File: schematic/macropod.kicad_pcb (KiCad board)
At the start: 2 copper layers, 97.5 x 113.5 mm, 52 parts, among them J1 USB_B_Micro, J2 Conn_ARM_JTAG_SWD_10, SW1 SW_MK, SW10 SW_MK, SW11 SW_MK, SW12 SW_MK, SW13 SW_MK, SW14 SW_MK, SW15 SW_MK, SW16 SW_MK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

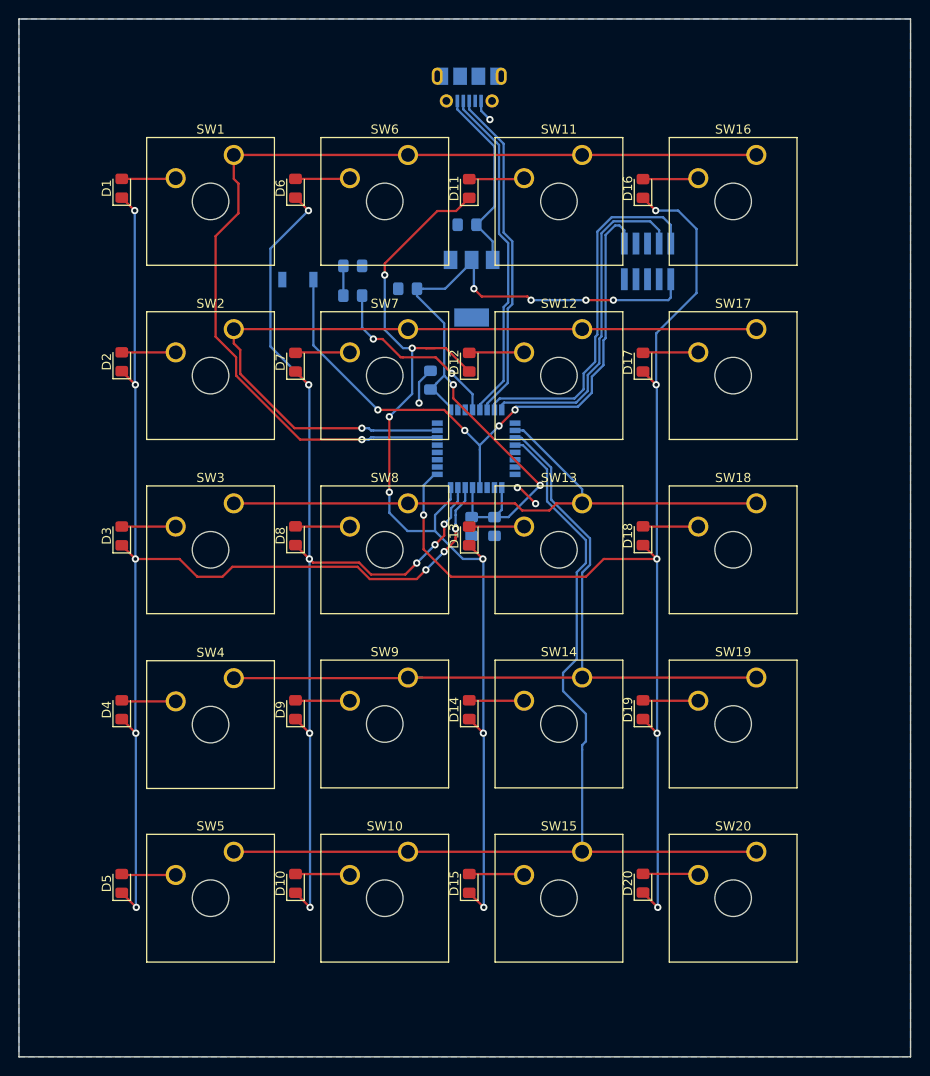
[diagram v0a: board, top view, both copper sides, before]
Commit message: Updated footprints to match BOM components. Applied DRC settings for fabrication
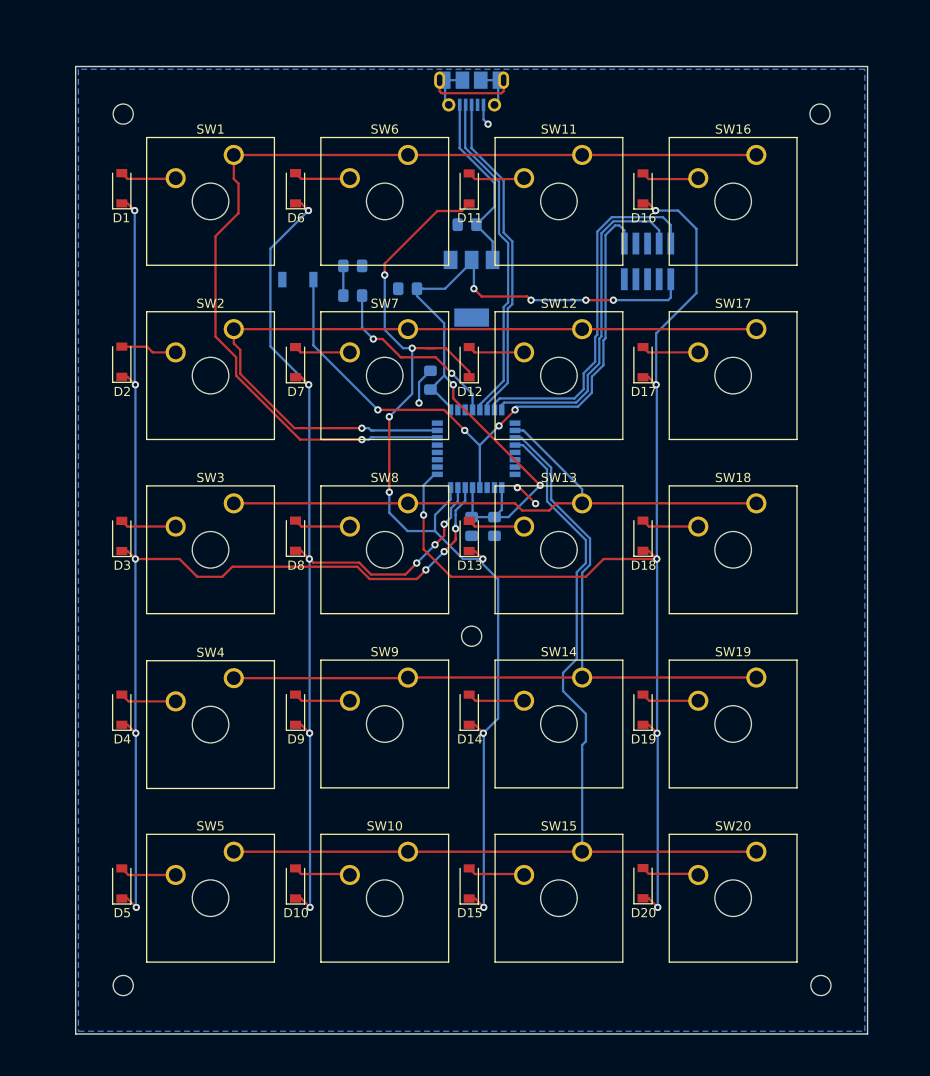
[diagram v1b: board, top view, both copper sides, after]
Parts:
- added M2_Mount1: MountingHole_2.2mm_M2, MountingHole:MountingHole_2.2mm_M2, B.Cu at (34.9, 33.6)
- added M2_Mount2: MountingHole_2.2mm_M2, MountingHole:MountingHole_2.2mm_M2, B.Cu at (34.9, 128.9)
- added M2_Mount3: MountingHole_2.2mm_M2, MountingHole:MountingHole_2.2mm_M2, B.Cu at (73.0, 90.7)
- added M2_Mount4: MountingHole_2.2mm_M2, MountingHole:MountingHole_2.2mm_M2, B.Cu at (111.1, 33.6)
- added M2_Mount5: MountingHole_2.2mm_M2, MountingHole:MountingHole_2.2mm_M2, B.Cu at (111.2, 128.9)
- D1, D10, D11, D12, D13, D14, D15, D16, D17, D18, D19, D2, D20, D3, D4, D5, D6, D7, D8, D9: footprint Diode_SMD:D_0805_2012Metric_Pad1.15x1.40mm_HandSolder -> Diode_SMD:D_SOD-123
- moved J1 0.50 mm to (73.0, 31.2)
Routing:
- net Net-(J1-Pad6): track 0.00 -> 19.1 mm
- net /ROW3: track 89.1 -> 87.6 mm
- net /COL3: track 128.6 -> 127.3 mm
- net /COL1: track 113.4 -> 112.1 mm
- net /COL0: track 132.7 -> 131.4 mm
- net /COL2: track 113.1 -> 114.1 mm
- net /USBD+: track 36.9 -> 36.2 mm
- net /VBUS: track 20.6 -> 20.1 mm
- net /USBD-: track 37.1 -> 36.6 mm
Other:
- board size 97.5 x 113.5 mm -> 86.6 x 105.8 mm
- board text added: "1"
- board text added: "10"
- board text added: "2"
- board text added: "2019-04-08"
- board text added: "9"
- board text added: "GND"
- board text added: "Macropod v1.0"
- board text added: "NRST"
- board text added: "SWCLK"
- board text added: "SWDIO"
- board text added: "VDD"
